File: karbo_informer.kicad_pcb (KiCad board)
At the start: 2 copper layers, 12 parts, among them IC1 MAX7219, IC2 MAX7219, P1 USB_OTG

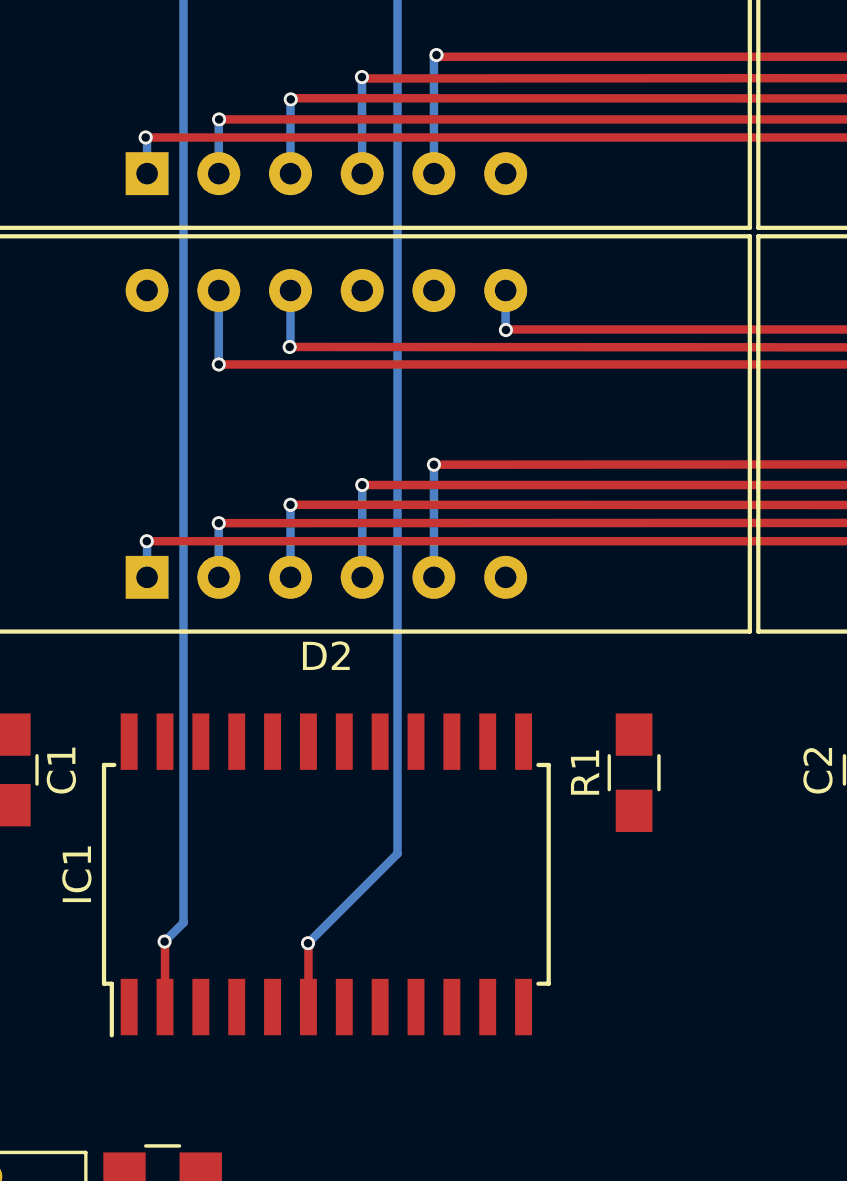
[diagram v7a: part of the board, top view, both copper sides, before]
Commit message: Wire for DIG3 to MAX7219 in the buy line
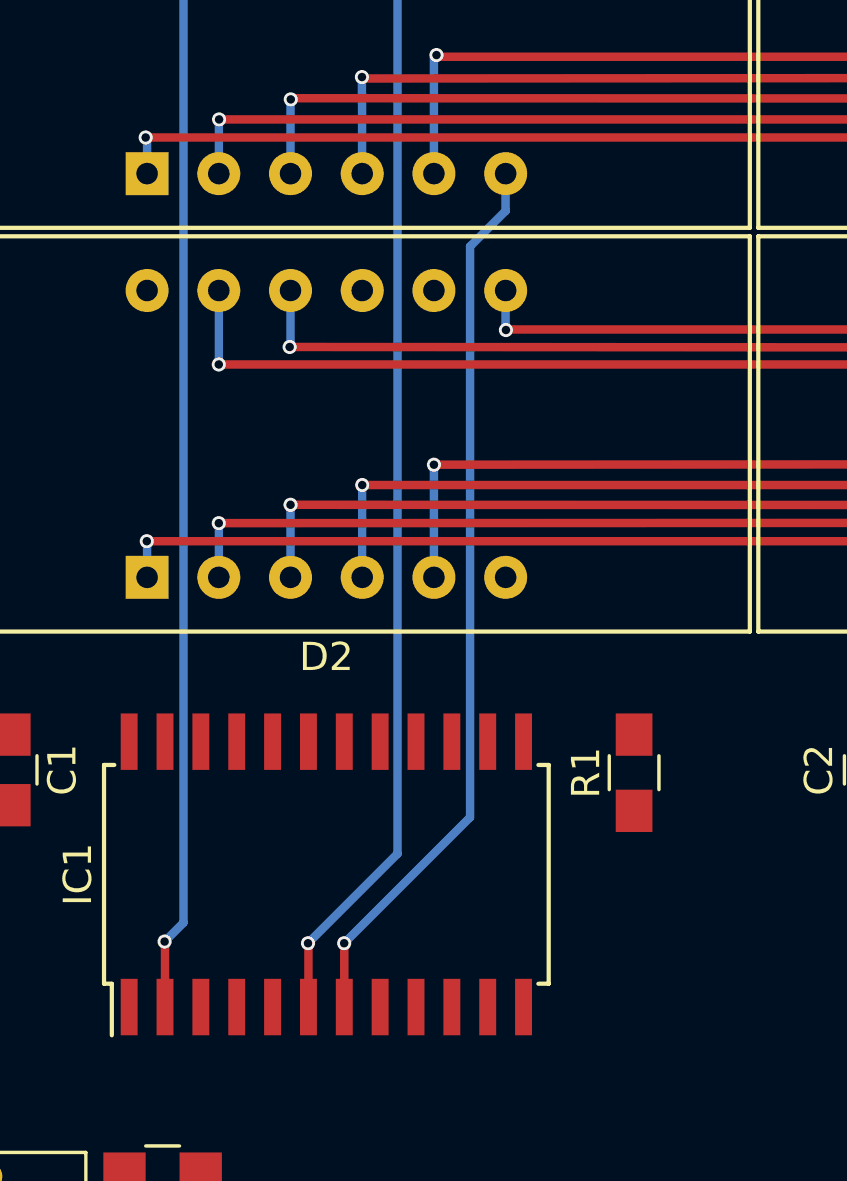
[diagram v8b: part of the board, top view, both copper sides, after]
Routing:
- net /B_DIG_3: track 0.00 -> 31.9 mm, vias 0 -> 1
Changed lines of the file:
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@@
   (general
     (links 69)
-    (no_connects 51)
+    (no_connects 50)
     (area 0 0 0 0)
     (thickness 1.6)
     (drawings 0)
-    (tracks 119)
+    (tracks 126)
     (zones 0)
     (modules 12)
@@
   (via (at 44.7 29.78) (size 0.5) (drill 0.3) (layers F.Cu B.Cu) (net 5))
   (segment (start 44.61 29.87) (end 44.7 29.78) (width 0.3) (layer B.Cu) (net 5))
+  (segment (start 47.15 33.98) (end 47.15 35.3) (width 0.3) (layer B.Cu) (net 6) (status 400000))
+  (segment (start 41.435 61.245) (end 41.435 63.5) (width 0.3) (layer F.Cu) (net 6) (status 800000))
+  (segment (start 41.43 61.24) (end 41.435 61.245) (width 0.3) (layer F.Cu) (net 6))
+  (via (at 41.43 61.24) (size 0.5) (drill 0.3) (layers F.Cu B.Cu) (net 6))
+  (segment (start 45.89 56.78) (end 41.43 61.24) (width 0.3) (layer B.Cu) (net 6))
+  (segment (start 45.89 36.56) (end 45.89 56.78) (width 0.3) (layer B.Cu) (net 6))
+  (segment (start 47.15 35.3) (end 45.89 36.56) (width 0.3) (layer B.Cu) (net 6))
   (segment (start 39.53 23.82) (end 39.54 25.87) (width 0.3) (layer B.Cu) (net 7))
   (segment (start 69.83 25.94) (end 69.83 23.82) (width 0.3) (layer B.Cu) (net 7))
